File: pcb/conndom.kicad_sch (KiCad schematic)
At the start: 17 parts, among them J1 5V, J10 USB A WIFI, J2 GND, J3 USB_DP, J4 USB_DM, J5 3V3, J6 GND, J7 PWR, J8 LED, J9 USB C PWR

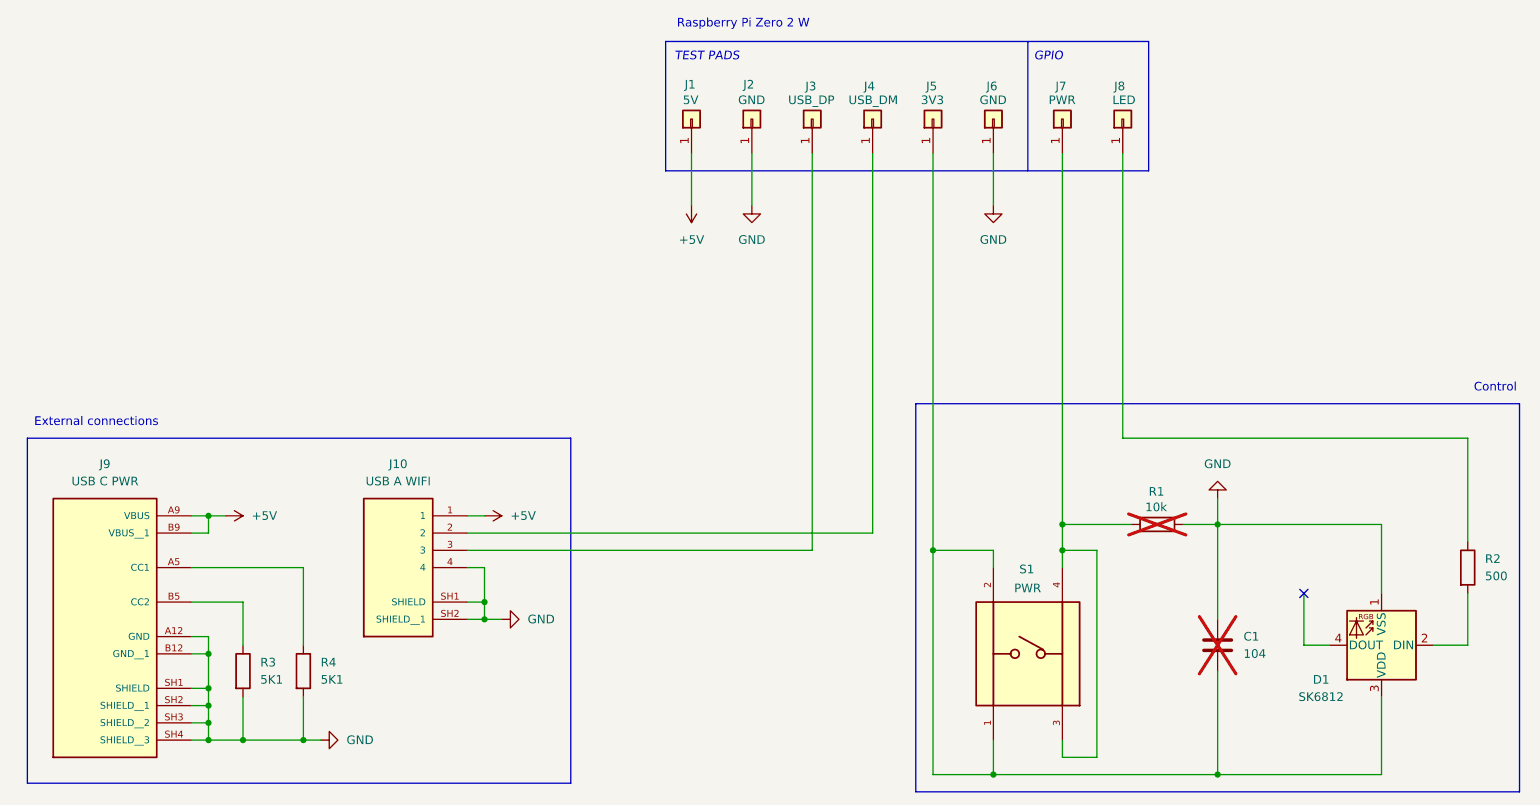
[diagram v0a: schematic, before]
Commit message: update footprints, renaming
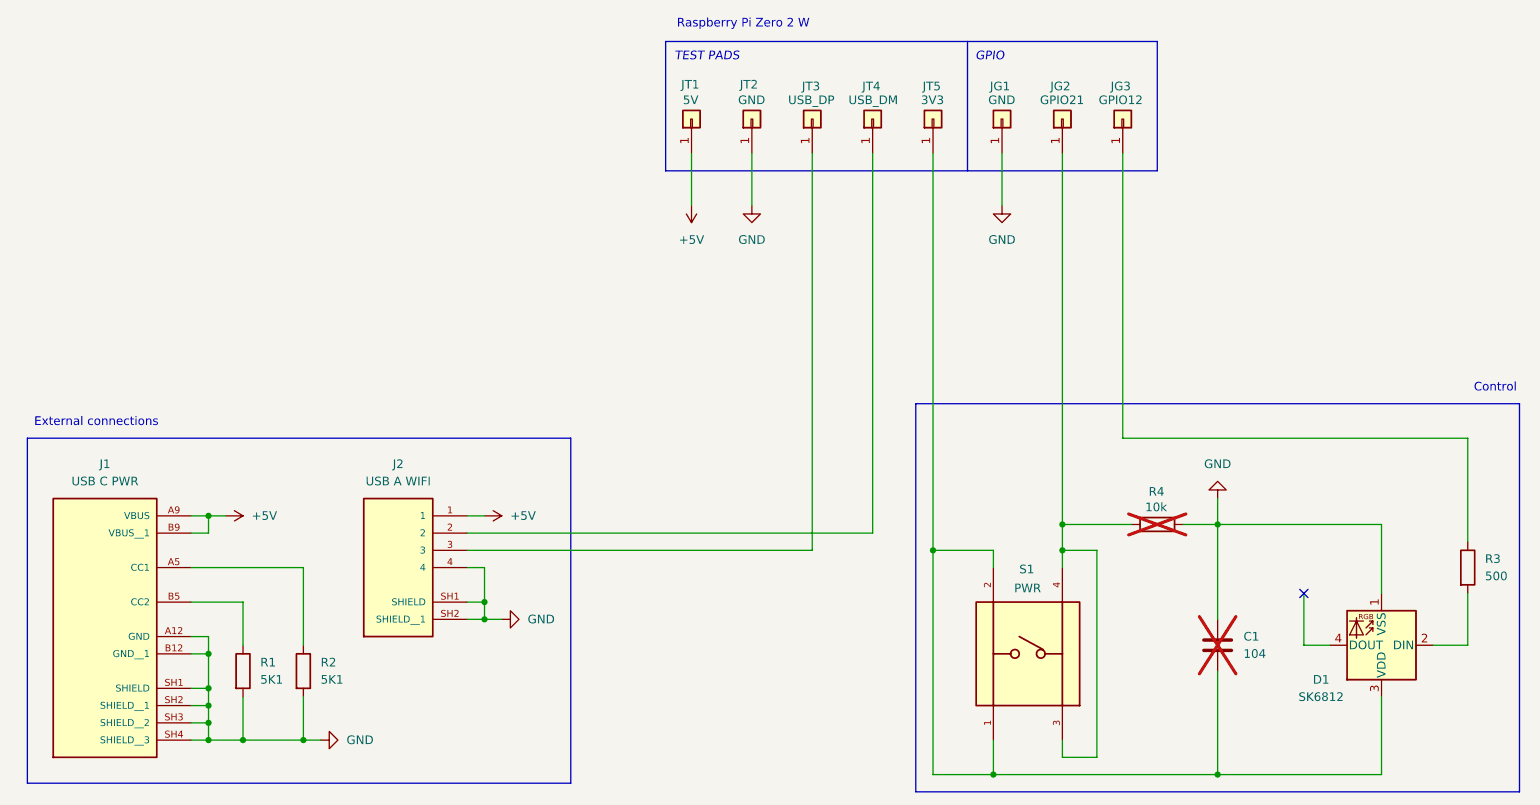
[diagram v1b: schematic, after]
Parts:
- JG1: renamed from J6; footprint rpi-zero-2-w-testpads:2mm-testpad-conn-plated -> rpi-zero-2-w-testpads:1.7mm-testpad-conn-plated
- JG2: renamed from J7; value PWR -> GPIO21
- JG3: renamed from J8; value LED -> GPIO12
- renumbered J9 to J1, J10 to J2, J1 to JT1, J2 to JT2, J3 to JT3, J4 to JT4, J5 to JT5, R3 to R1, R4 to R2, R2 to R3, R1 to R4
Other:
- title: (none) -> conndom
- moved on the sheet: JG1

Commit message: bom excludes
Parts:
- JG1, JG2, JG3, JT1, JT2, JT3, JT4, JT5: now left out of the parts list
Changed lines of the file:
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@@
 		(unit 1)
 		(exclude_from_sim no)
-		(in_bom yes)
+		(in_bom no)
 		(on_board yes)
 		(dnp no)
@@
 		(unit 1)
 		(exclude_from_sim no)
-		(in_bom yes)
+		(in_bom no)
 		(on_board yes)
 		(dnp no)
@@
 		(unit 1)
 		(exclude_from_sim no)
-		(in_bom yes)
+		(in_bom no)
 		(on_board yes)
 		(dnp no)
@@
 		(unit 1)
 		(exclude_from_sim no)
-		(in_bom yes)
+		(in_bom no)
 		(on_board yes)
 		(dnp no)
@@
 		(unit 1)
 		(exclude_from_sim no)
-		(in_bom yes)
+		(in_bom no)
 		(on_board yes)
 		(dnp no)
@@
 		(unit 1)
 		(exclude_from_sim no)
-		(in_bom yes)
+		(in_bom no)
 		(on_board yes)
 		(dnp no)
@@
 		(unit 1)
 		(exclude_from_sim no)
-		(in_bom yes)
+		(in_bom no)
 		(on_board yes)
 		(dnp no)
@@
 		(unit 1)
 		(exclude_from_sim no)
-		(in_bom yes)
-		(on_board yes)
-		(dnp no)
+		(in_bom no)
+		(on_board yes)
+		(dnp no)
